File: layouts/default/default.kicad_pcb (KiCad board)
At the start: 4 copper layers, 60 x 48 mm, 54 parts

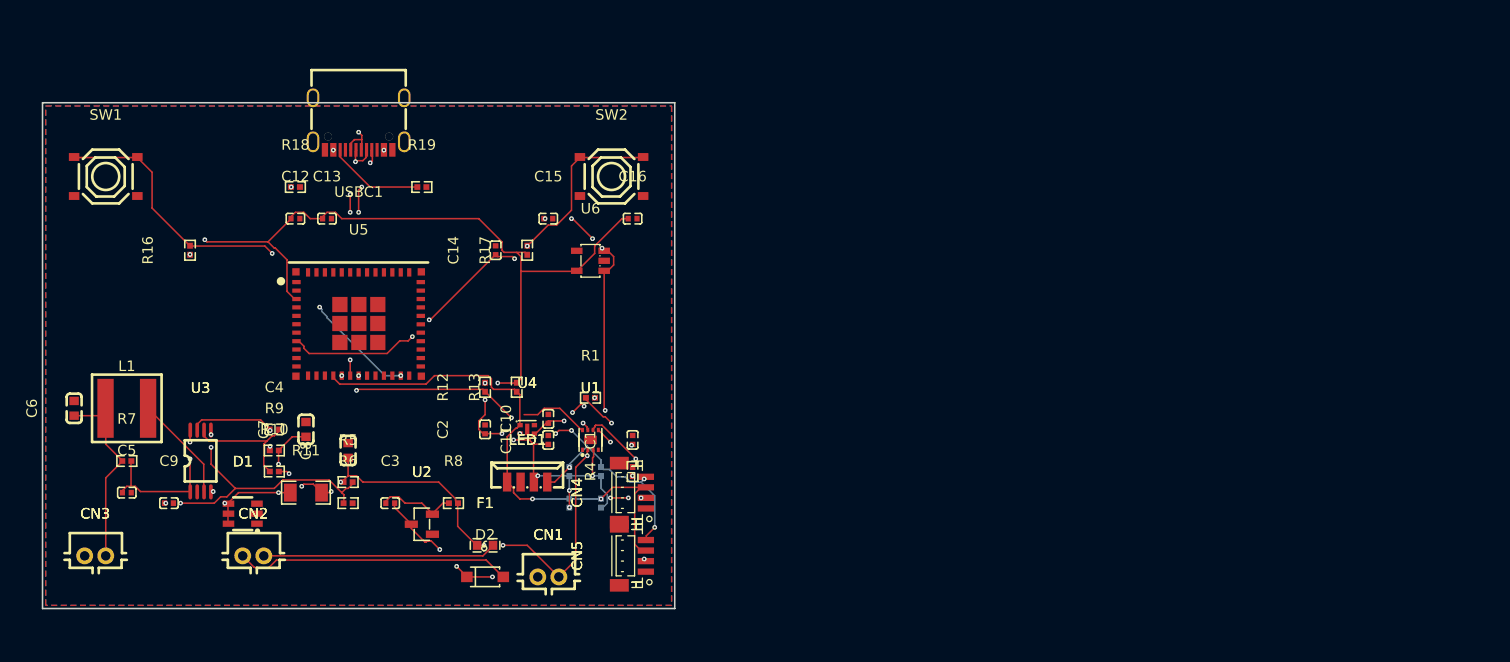
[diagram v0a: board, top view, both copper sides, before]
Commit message: Add OpenSCAD enclosure, STEP exports, PCB previews, and Quilter candidates
- Add OpenSCAD parametric enclosure (enclosure.scad) with full assembly exports
- Add STEP export pipeline (export_all.py) with assembly components
- Add STL/STEP files for base, lid, ball/nut/socket hardware
- Add 3MF print files for hardware parts
- Add PCB preview PDF/SVG for default layout
- Add Quilter 4-layer and 6-layer PCB candidates
- Add setup_board.py for board setup automation
- Update enclosure.py and view_enclosure.py (build123d)
- Update main.ato and micromppt.ato (circuit refinements)
- Update prepare_for_quilter.py and ato.yaml
- Add docs/power_budget.md

Co-Authored-By: Claude Sonnet 4.6 <noreply@anthropic.com>
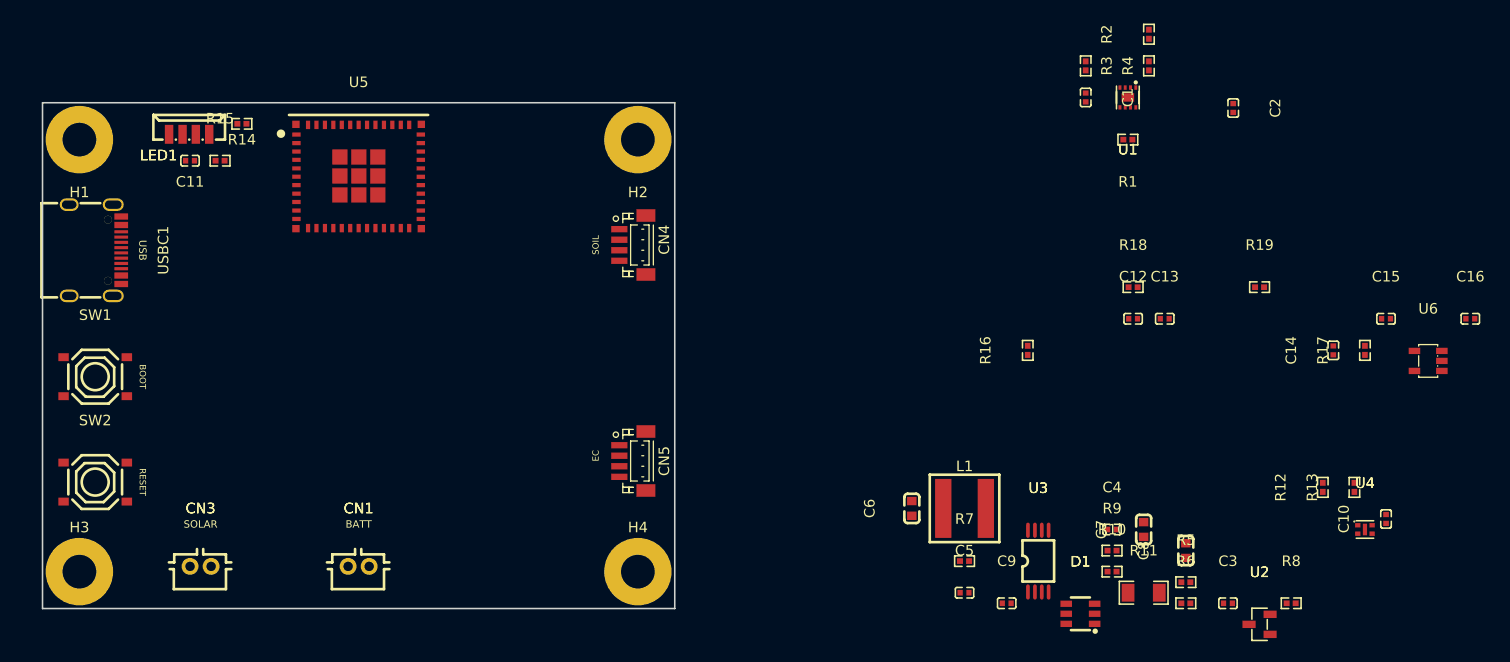
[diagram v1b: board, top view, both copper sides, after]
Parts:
- removed CN2: , JST_Sales_America_B2B_PH_K_S_LF__SN:CONN-TH_B2B-PH-K-S
- removed D2: Vf ℝ+V, GOODWORK_B5819W:SOD-123F_L2.7-W1.6-LS3.8-RD-1
- removed F1: , Littelfuse_0603L150SLYR:F0603
- added H1: , MountingHole_3_2_M3:MountingHole_3.2_M3, F.Cu at (103.5, 81.5)
- added H2: , MountingHole_3_2_M3:MountingHole_3.2_M3, F.Cu at (156.5, 81.5)
- added H3: , MountingHole_3_2_M3:MountingHole_3.2_M3, F.Cu at (103.5, 122.5)
- added H4: , MountingHole_3_2_M3:MountingHole_3.2_M3, F.Cu at (156.5, 122.5)
- R14, R15, R2, R3: moved to F.Cu
- moved C10 80.1 mm to (227.5, 117.5)
- moved C12 80.1 mm to (203.5, 98.5)
- moved C13 80.1 mm to (206.5, 98.5)
- moved C14 80.1 mm to (222.5, 101.5)
- moved C15 80.1 mm to (227.5, 98.5)
- moved C16 80.1 mm to (235.5, 98.5)
- moved C3 80.1 mm to (212.5, 125.5)
- moved C4 80.1 mm to (201.5, 118.5)
- moved C5 80.1 mm to (187.5, 124.5)
- moved C6 80.1 mm to (182.5, 116.5)
- moved C7 80.1 mm to (204.5, 118.5)
- moved C8 80.1 mm to (208.5, 120.5)
- moved C9 80.1 mm to (191.5, 125.5)
- moved D1 80.1 mm to (198.5, 126.5)
- moved L1 80.1 mm to (187.5, 116.5)
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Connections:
- net cathode renamed Vbatr-lv
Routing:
- net hv: track 121.6 -> 0.00 mm, vias 19 -> 0
- net Vbatr-hv: track 80.8 -> 0.00 mm, vias 13 -> 0
- net SDA: track 57.0 -> 0.00 mm, vias 2 -> 0
- net SCL: track 48.8 -> 0.00 mm, vias 10 -> 0
- net c_en-power-hv: track 44.2 -> 0.00 mm, vias 4 -> 0
- net A: track 42.3 -> 0.00 mm, vias 3 -> 0
- net 18: track 29.0 -> 0.00 mm, vias 4 -> 0
- net Coutsns-power-hv: track 27.4 -> 0.00 mm, vias 4 -> 0
- net anode: track 26.1 -> 0.00 mm
- net 17: track 23.6 -> 0.00 mm, vias 4 -> 0
- net 1: track 22.3 -> 0.00 mm
- net Vpvr-hv: track 18.4 -> 0.00 mm
- net Cout1-power-hv: track 18.0 -> 0.00 mm, vias 4 -> 0
- net Vbatr-lv: track 17.1 -> 0.00 mm, vias 3 -> 0
- net Cinsns-power-hv: track 15.3 -> 0.00 mm, vias 2 -> 0
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- removed copper zone on B.Cu, net lv
- removed copper zone on F.Cu, net lv
- removed copper zone on In1.Cu, net lv
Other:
- board text added: "BATT"
- board text added: "BOOT"
- board text added: "EC"
- board text added: "RESET"
- board text added: "SOIL"
- board text added: "SOLAR"
- board text added: "USB"

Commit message: feat: add external NTC thermistor (ADS1115) and place all components on 60x48mm board
Add high-precision external NTC temperature measurement circuit using
ADS1115 16-bit ADC (I2C addr 0x48) with 10k 0.1% reference resistor
and JST PH 2-pin probe connector. This addresses solar heating bias
on the onboard SHT40 sensor — the metal-tip NTC probe protrudes from
the enclosure for true ambient temperature (0.1°C resolution).

Also place all 64 components on the 60x48mm 4-layer PCB following the
placement strategy: MPPT top-left, LDO center, ESP32-C6 top-right
(antenna toward board edge), sensors bottom-left, fuel gauge center,
USB-C and Qwiic bottom-right.

New files:
- ntc_adc.ato: ADS1115 + precision R_ref + NTC connector module
- loadswitch.ato: GPIO-controlled P-FET high-side switch
- parts/Texas_Instruments_ADS1115IRUGR/: ADS1115 package (LCSC C2651328)
- parts/YAGEO_RT0402BRD0710KL/: 10k 0.1% precision resistor (LCSC C190095)
- scripts/place_components.py: automated PCB placement script
- docs/pcb_placement_strategy.md: placement strategy with floor plan

Co-Authored-By: Claude Opus 4.6 (1M context) <noreply@anthropic.com>
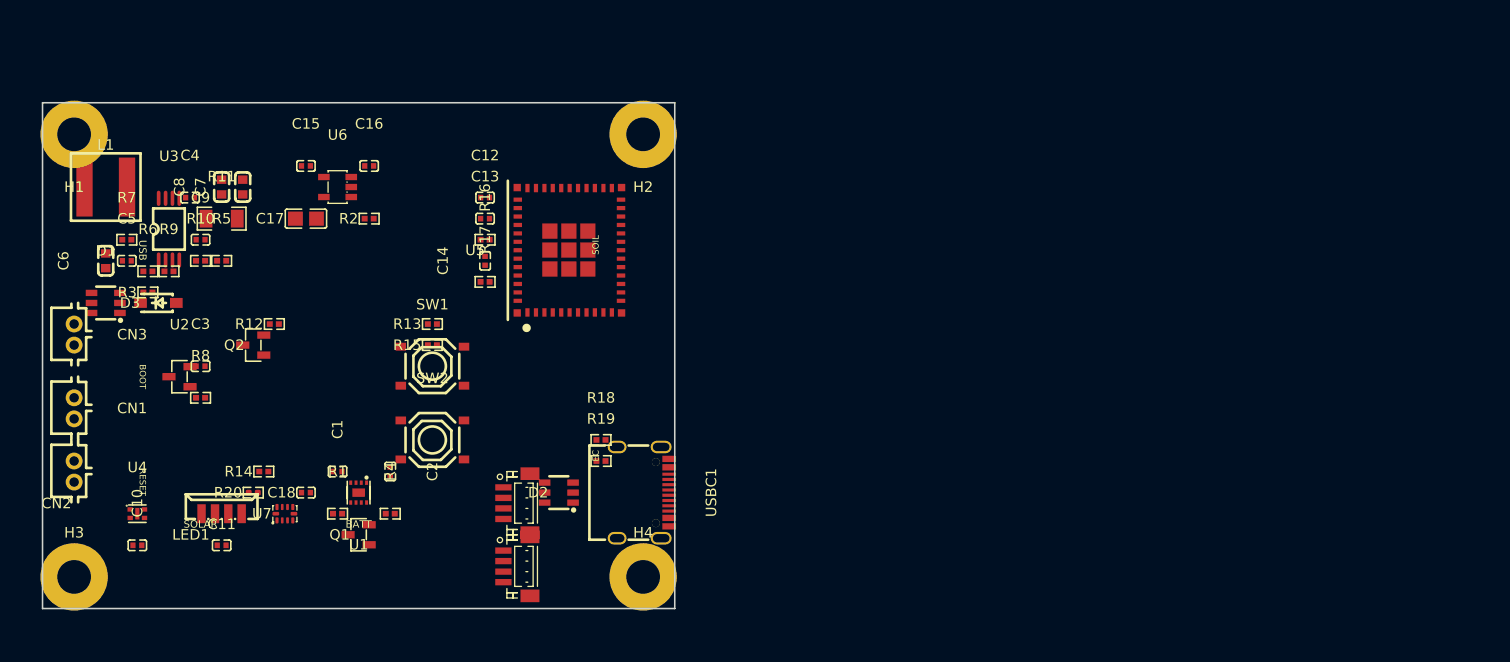
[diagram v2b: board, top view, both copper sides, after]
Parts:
- added C17: 100µF ±20%, Murata_Electronics_GRM21BR60J107ME15L:C0805, F.Cu at (125.0, 89.0)
- added C18: 100nF ±10%, Samsung_Electro_Mechanics_CL05B104KO5NNNC:C0402, F.Cu at (125.0, 115.0)
- added CN2: , JST_Sales_America_B2B_PH_K_S_LF__SN:CONN-TH_B2B-PH-K-S, F.Cu at (103.0, 113.0)
- added D2: , TECH_PUBLIC_SRV05_4_P_T7:SOT-23-6_L2.9-W1.6-P0.95-LS2.8-BR, F.Cu at (149.0, 115.0)
- added D3: Vf {ℝ+}V, Changjiang_Electronics_Tech_B5819W_SL:SOD-123_L2.7-W1.6-LS3.7-RD-1, F.Cu at (111.0, 97.0)
- added Q1: , XySemi_XB3306D:SOT-23-3_L2.9-W1.3-P1.90-LS2.4-BR, F.Cu at (130.0, 119.0)
- added Q2: , XySemi_XB3306D:SOT-23-3_L2.9-W1.3-P1.90-LS2.4-BR, F.Cu at (120.0, 101.0)
- added R20: , YAGEO_RT0402BRD0710KL:R0402, F.Cu at (120.0, 115.0)
- added U7: , Texas_Instruments_ADS1115IRUGR:X2QFN-10_L2.0-W1.5-P0.50-BL, F.Cu at (123.0, 117.0)
- C1, C14, C15, C16, C2, C4: value 0F -> 1µF ±10%
- C10, C11, C13, C3, C5: value 0F -> 100nF ±10%
- C12: value 0F -> 10µF ±20%
- C6, C8: value 0F -> 10µF ±10%
- C7: value 0F -> 4.7µF ±10%
- C9: value 0F -> 1nF ±10%
- L1: value L ℝ+H -> L {ℝ+}H
- R1, R13, R15, R16, R17, R4: value 10000Ω -> 10kΩ ±1%
- R10, R7, R9: value 1000Ω -> 1kΩ ±1%
- R11: value 0.01Ω -> 10mΩ ±1%
- R12, R14: value 10000Ω -> 100kΩ ±1%; footprint UNI_ROYAL_0402WGF1002TCE:R0402 -> UNI_ROYAL_0402WGF1003TCE:R0402
- R18, R19: value 5100Ω -> 5.1kΩ ±1%
- R2, R3: value 10000Ω -> 2.2kΩ ±1%; footprint UNI_ROYAL_0402WGF1002TCE:R0402 -> UNI_ROYAL_0402WGF2201TCE:R0402
- R5: value 1000000Ω -> 1MΩ ±1%
- R6: value 450000Ω -> 422kΩ ±1%; footprint FOJAN_FRC0402F4503TS:R0402 -> YAGEO_AF0402FR_07422KL:R0402
- R8: value 100Ω -> 100Ω ±1%
- moved C10 118.5 mm to (109.0, 120.0), turned to 0 degrees
- moved U4 116.5 mm to (109.0, 117.0)
- moved C16 105.5 mm to (131.0, 84.0)
- moved R8 105.3 mm to (115.0, 106.0)
- moved U2 105.2 mm to (113.0, 104.0)
- moved U6 104.8 mm to (128.0, 86.0)
- moved C15 103.5 mm to (125.0, 84.0)
- moved R6 103.4 mm to (110.0, 94.0)
- moved R12 100.7 mm to (122.0, 99.0), turned to 0 degrees
- moved C3 100.1 mm to (115.0, 103.0)
- moved C8 97.8 mm to (117.0, 86.0)
- moved R3 97.4 mm to (110.0, 96.0), turned to 0 degrees
- moved D1 97.1 mm to (106.0, 97.0)
- moved R5 96.4 mm to (117.0, 93.0)
- moved R11 94.4 mm to (117.0, 89.0)
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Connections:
- C1 pad 1: Vbatr-hv -> hv
- C15 pad 1: Vbatr-hv -> hv
- C6 pad 1: Vpvr-hv -> cathode
- C8 pad 1: Vbatr-hv -> hv
- CN1 pad 1: Vbatr-hv -> hv
- CN3 pad 1: Vpvr-hv -> anode
- L1 pad 1: Vpvr-hv -> cathode
- R1 pad 1: nALRT -> 5
- R10 pad 2: Vbatr-hv -> hv
- R11 pad 2: Vbatr-hv -> hv
- R12 pad 1: SCL -> hv
- R12 pad 2: hv -> G
- R13 pad 1: SDA -> line
- R13 pad 2: hv -> G
- R14 pad 2: SCL -> sensor_gate-G
- R15 pad 1: hv -> sensor_gate-enable-line
- R15 pad 2: SDA -> sensor_gate-G
- R5 pad 1: Vbatr-hv -> hv
- R7 pad 1: Vpvr-hv -> cathode
- R8 pad 2: Vbatr-hv -> hv
- U1 pad 2: Vbatr-hv -> hv
- U1 pad 5: nALRT -> 5
- U5 pad 12: 12 -> line
- U5 pad 13: 13 -> sensor_gate-enable-line
- U6 pad 1: Vbatr-hv -> hv
- U6 pad 3: Vbatr-hv -> hv
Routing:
- added copper zone on In2.Cu, net hv
- added copper zone on In1.Cu, net lv
